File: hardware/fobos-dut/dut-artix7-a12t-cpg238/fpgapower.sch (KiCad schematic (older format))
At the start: 30 parts, among them U1 XC7A12T-CPG238

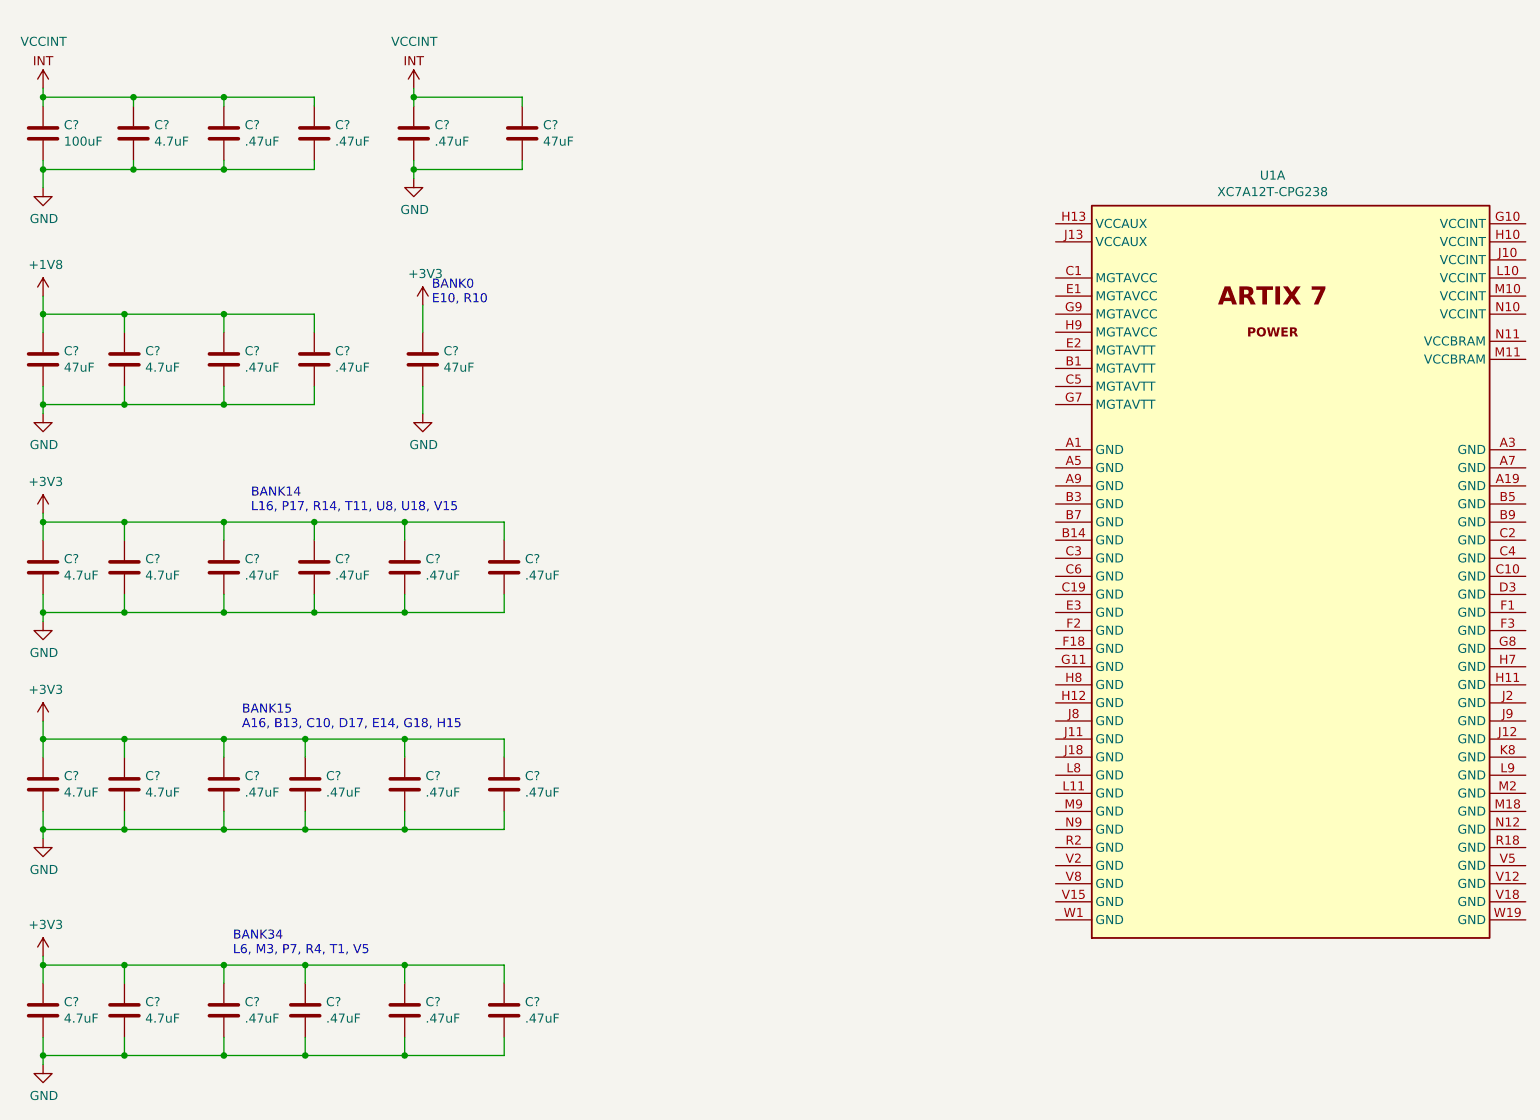
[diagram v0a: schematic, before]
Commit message: Connected the fixed signals to the FPGA, flexible IO are left unconnected Added 0.1 ohm resistors to the 1V8 and 3V3 power rails, added test points which allow for easy measurement Updated ARTIX7-A12T-CPG238 symbol to make schematic route similarly to the last symbol Connected CFGVBS signal to the 3V3 rail, was previously connected to VCCINT which was a mistake Ran through 7 Series schematic review checklist - 7_Series_Schematic_Review_Recommendations.xlsm Added Xilinx pinout files for the CPG238 package Generated schematic for the csg325 for easy referencing
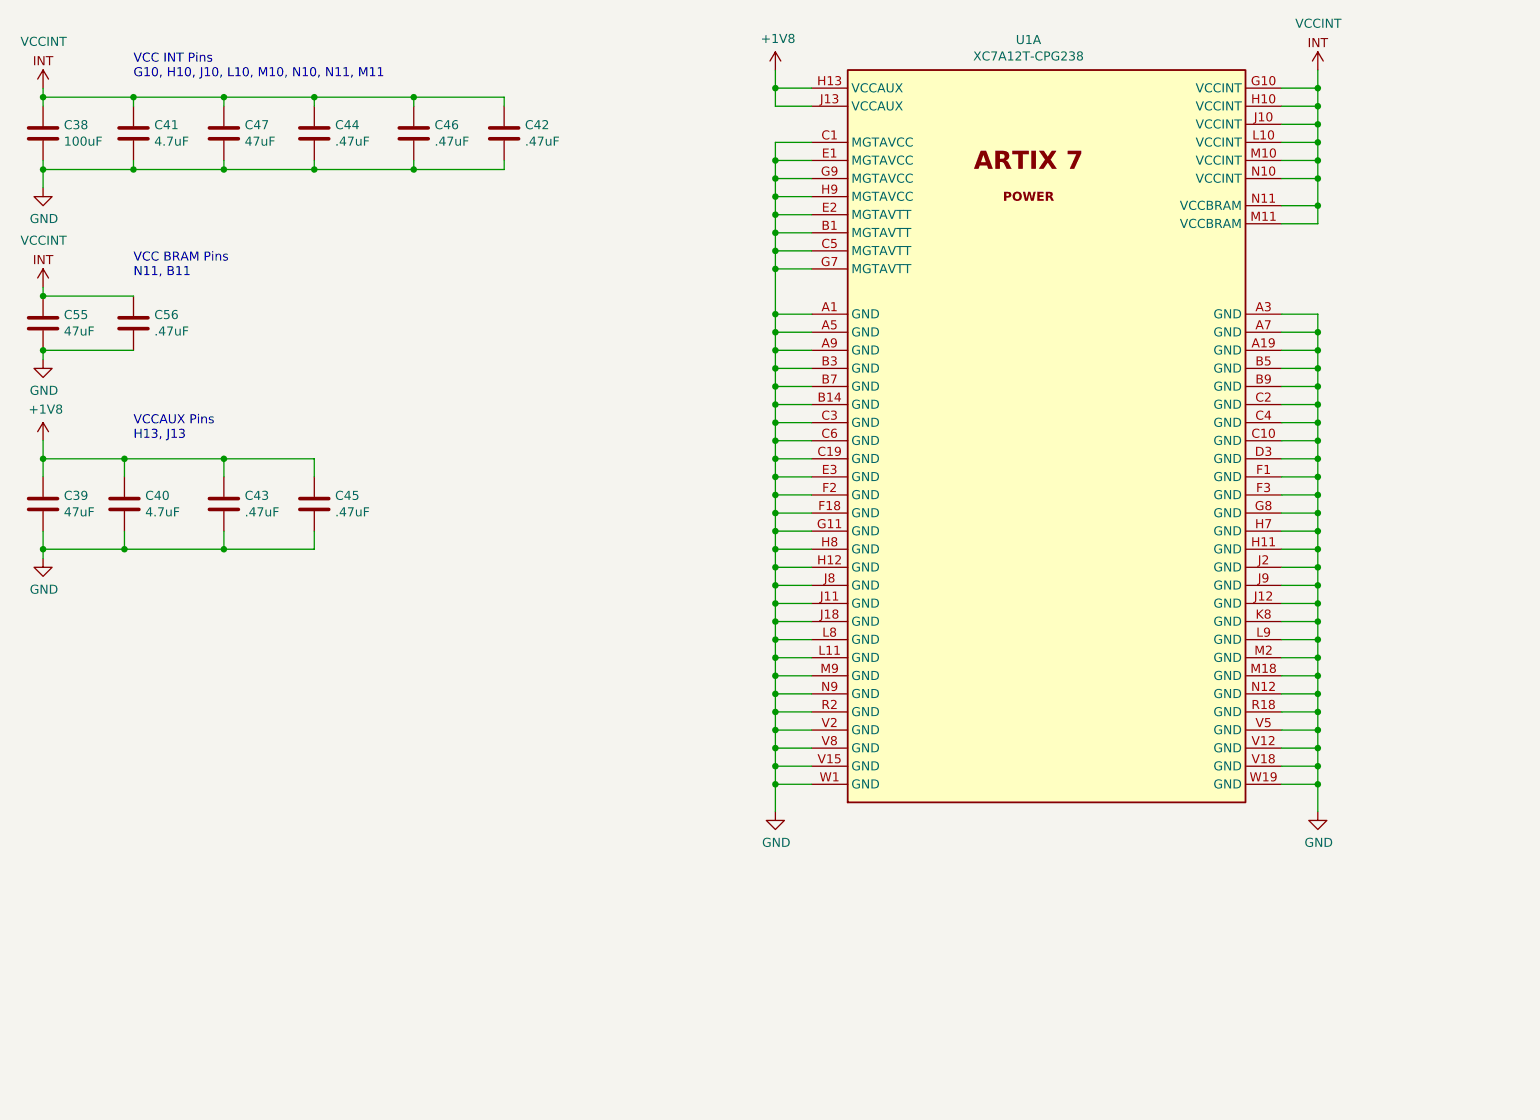
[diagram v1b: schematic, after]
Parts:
- removed C?: 47uF, Capacitor_SMD:C_0603_1608Metric_Pad1.08x0.95mm_HandSolder, symbol Device:C
- removed C? (x6): 4.7uF, Capacitor_SMD:C_0402_1005Metric_Pad0.74x0.62mm_HandSolder, symbol Device:C
- removed C? (x12): .47uF, Capacitor_SMD:C_0402_1005Metric_Pad0.74x0.62mm_HandSolder, symbol Device:C
- added C55: 47uF, Capacitor_SMD:C_0603_1608Metric_Pad1.08x0.95mm_HandSolder, symbol Device:C
- added C56: .47uF, Capacitor_SMD:C_0402_1005Metric_Pad0.74x0.62mm_HandSolder, symbol Device:C
- gave numbers to parts that had none: 10
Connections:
- net +1V8: now also U1.H13 (VCCAUX), U1.J13 (VCCAUX)
- net GND: now also U1.A1 (GND), U1.A19 (GND), U1.A3 (GND), U1.A5 (GND), U1.A7 (GND), U1.A9 (GND), U1.B1 (MGTAVTT), U1.B14 (GND), U1.B3 (GND), U1.B5 (GND), U1.B7 (GND), U1.B9 (GND), U1.C1 (MGTAVCC), U1.C10 (GND), U1.C19 (GND), U1.C2 (GND), U1.C3 (GND), U1.C4 (GND), U1.C5 (MGTAVTT), U1.C6 (GND), U1.D3 (GND), U1.E1 (MGTAVCC), U1.E2 (MGTAVTT), U1.E3 (GND), U1.F1 (GND), U1.F18 (GND), U1.F2 (GND), U1.F3 (GND), U1.G11 (GND), U1.G7 (MGTAVTT), U1.G8 (GND), U1.G9 (MGTAVCC), U1.H11 (GND), U1.H12 (GND), U1.H7 (GND), U1.H8 (GND), U1.H9 (MGTAVCC), U1.J11 (GND), U1.J12 (GND), U1.J18 (GND), U1.J2 (GND), U1.J8 (GND), U1.J9 (GND), U1.K8 (GND), U1.L11 (GND), U1.L8 (GND), U1.L9 (GND), U1.M18 (GND), U1.M2 (GND), U1.M9 (GND), U1.N12 (GND), U1.N9 (GND), U1.R18 (GND), U1.R2 (GND), U1.V12 (GND), U1.V15 (GND), U1.V18 (GND), U1.V2 (GND), U1.V5 (GND), U1.V8 (GND), U1.W1 (GND), U1.W19 (GND), C55.2, C56.2
- net VCCINT: now also U1.G10 (VCCINT), U1.H10 (VCCINT), U1.J10 (VCCINT), U1.L10 (VCCINT), U1.M10 (VCCINT), U1.M11 (VCCBRAM), U1.N10 (VCCINT), U1.N11 (VCCBRAM), C55.1, C56.1
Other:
- note added: "VCC BRAM Pins\nN11, B11\n"
- note added: "VCC INT Pins\nG10, H10, J10, L10, M10, N10, N11, M11"
- note added: "VCCAUX Pins\nH13, J13"
- note removed: "BANK0\nE10, R10"
- note removed: "BANK14\nL16, P17, R14, T11, U8, U18, V15"
- note removed: "BANK15\nA16, B13, C10, D17, E14, G18, H15"
- note removed: "BANK34\nL6, M3, P7, R4, T1, V5"
- moved on the sheet: C39, C40, C42, C43, C45, C47, U1A

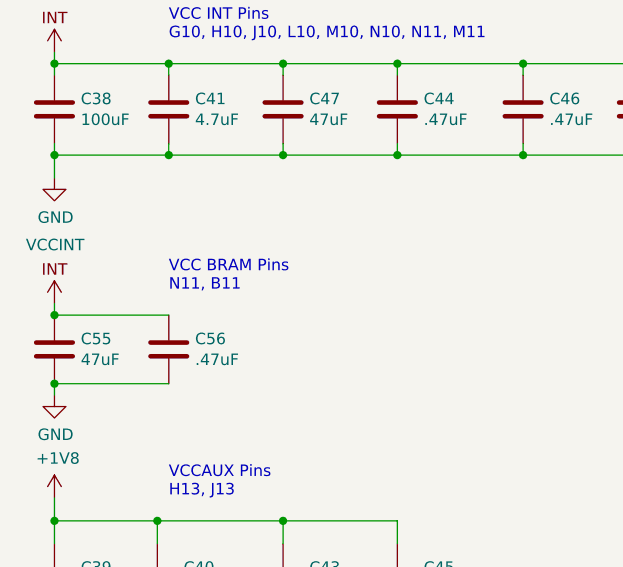
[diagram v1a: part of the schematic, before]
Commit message: Moved bypass/coupling capacitors underneath the FPGA Started routing top layer using 10 mil tracks with 5 mil spacing
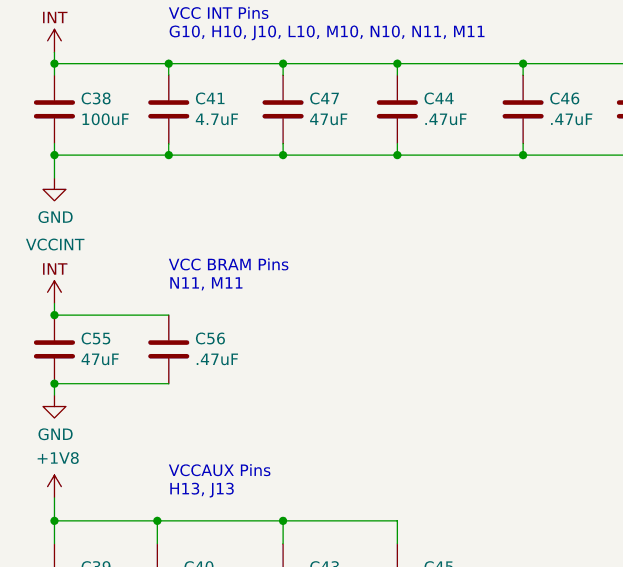
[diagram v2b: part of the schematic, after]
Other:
- note added: "VCC BRAM Pins\nN11, M11\n"
- note removed: "VCC BRAM Pins\nN11, B11\n"
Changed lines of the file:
@@
 Connection ~ 1150 2700
 Text Notes 1650 2600 0    50   ~ 0
-VCC BRAM Pins\nN11, B11\n
+VCC BRAM Pins\nN11, M11\n
 Text Notes 1650 3500 0    50   ~ 0
 VCCAUX Pins\nH13, J13
